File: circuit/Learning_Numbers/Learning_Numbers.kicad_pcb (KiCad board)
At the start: 2 copper layers, 141 x 124 mm, 106 parts, among them SW1 SW_DIP_x01, SW10 SW_Push, SW11 SW_Push, SW12 SW_Push, SW13 SW_Push, SW14 SW_Push, SW15 SW_Push, SW16 SW_Push, SW17 SW_Push, SW18 SW_Push, SW19 SW_Push, SW2 SW_Push, SW20 SW_Push, SW21 SW_Push, SW22 SW_Push, SW23 SW_Push, SW3 SW_Push, SW4 SW_Push, SW5 SW_Push, SW6 SW_Push, SW7 SW_Push, SW8 SW_Push, SW9 SW_Push, U1 ATmega168PA-P, U2 74HC165, U3 74HC165, U4 74HC595, U5 74HC595, U6 74HC595, U7 74HC595, U8 74HC595

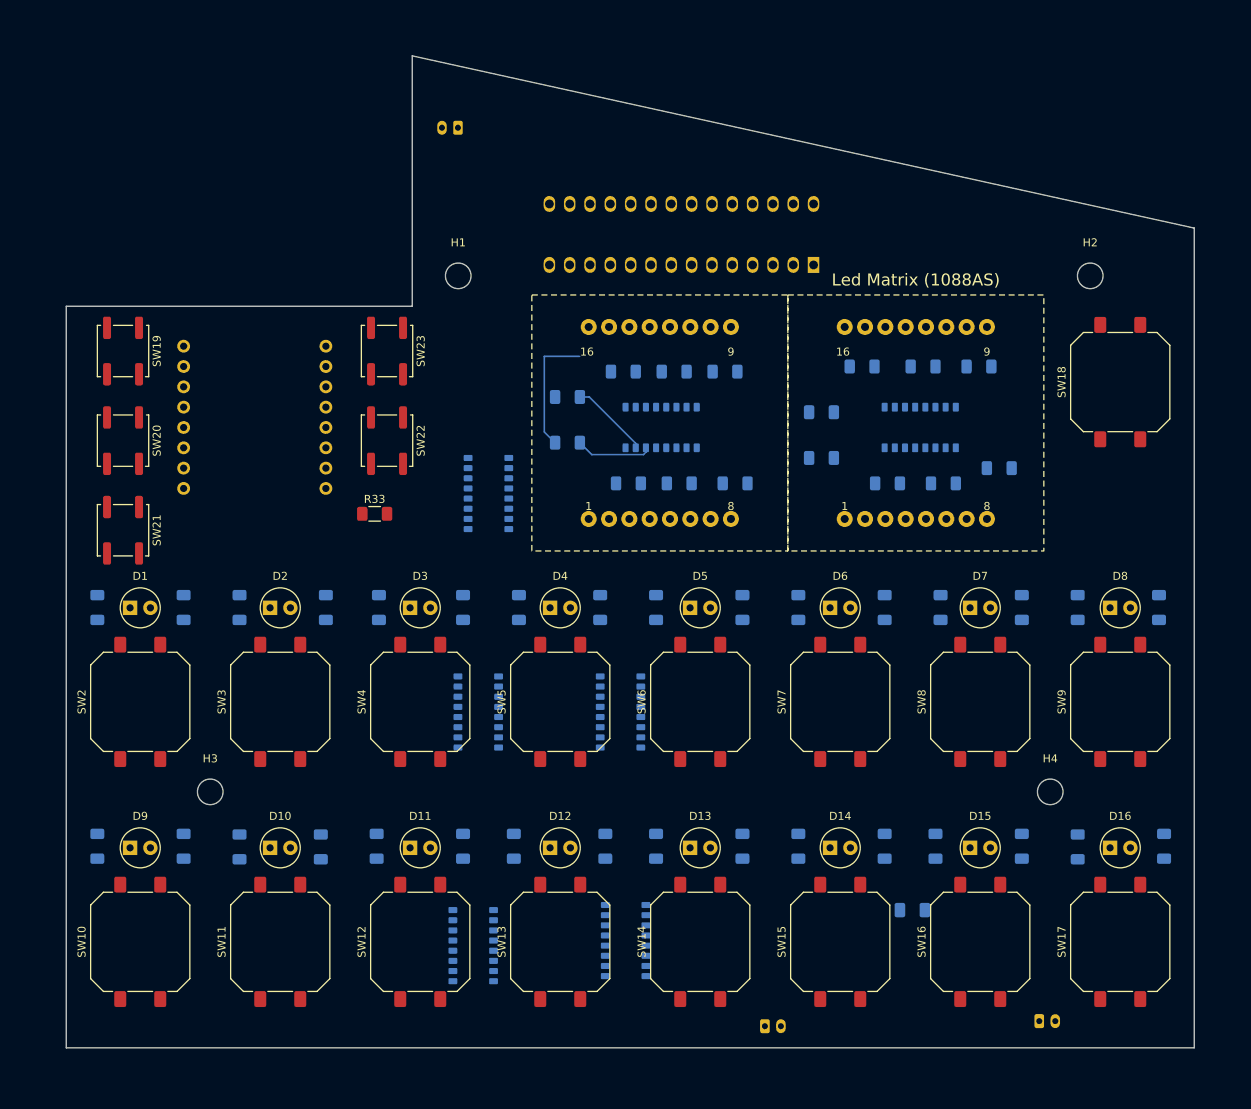
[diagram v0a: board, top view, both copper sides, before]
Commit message: finish circuit pathing
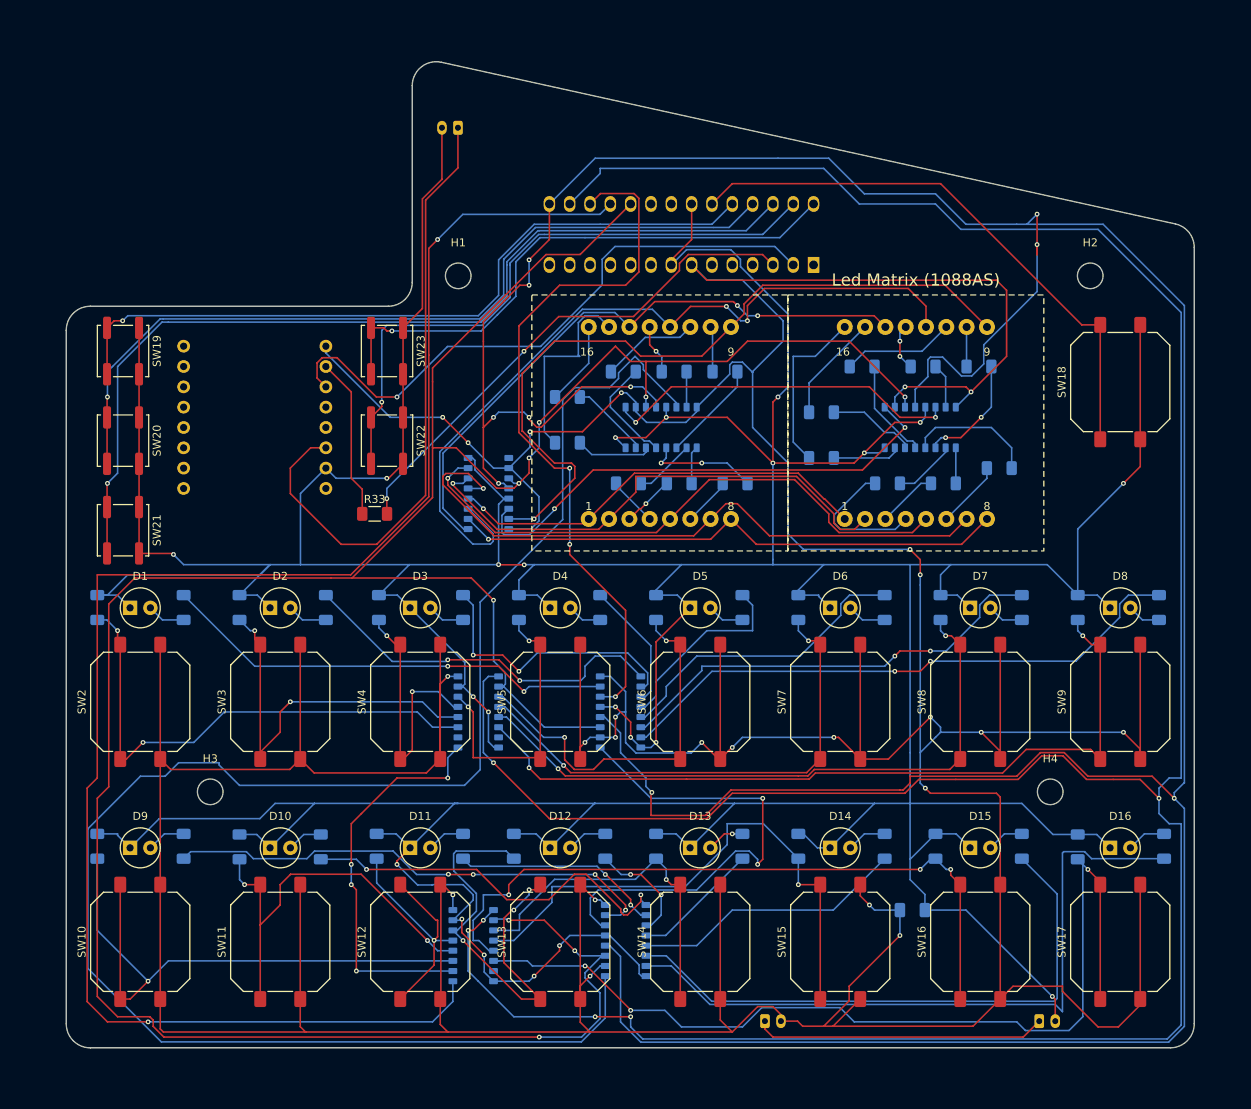
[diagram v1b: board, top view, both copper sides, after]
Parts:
- moved SW1 0.63 mm to (139.3, 158.7)
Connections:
- U4 pad 12: unconnected-(U4-RCLK-Pad12) -> LATCH
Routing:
- net GND: track 0.00 -> 851.2 mm, vias 0 -> 22
- net VCC: track 0.00 -> 846.9 mm, vias 0 -> 24
- net LATCH: track 0.00 -> 460.4 mm, vias 0 -> 10
- net PL: track 0.00 -> 387.1 mm, vias 0 -> 6
- net CLOCK: track 0.00 -> 367.8 mm, vias 0 -> 9
- net Net-(U4-SER): track 0.00 -> 217.7 mm
- net Net-(U1-PB4): track 0.00 -> 205.8 mm, vias 0 -> 2
- net Switch16: track 0.00 -> 119.2 mm, vias 0 -> 3
- net PC3: track 0.00 -> 116.8 mm, vias 0 -> 1
- net PC2: track 0.00 -> 103.5 mm, vias 0 -> 1
- net Switch8: track 0.00 -> 99.9 mm, vias 0 -> 2
- net row4: track 0.00 -> 98.5 mm, vias 0 -> 2
- net row1: track 0.00 -> 94.6 mm, vias 0 -> 1
- net PC1: track 0.00 -> 93.0 mm, vias 0 -> 1
- net SER: track 0.00 -> 89.3 mm, vias 0 -> 3
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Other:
- board size 141 x 124 mm -> 141 x 123.3 mm

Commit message: add crystal to circuit
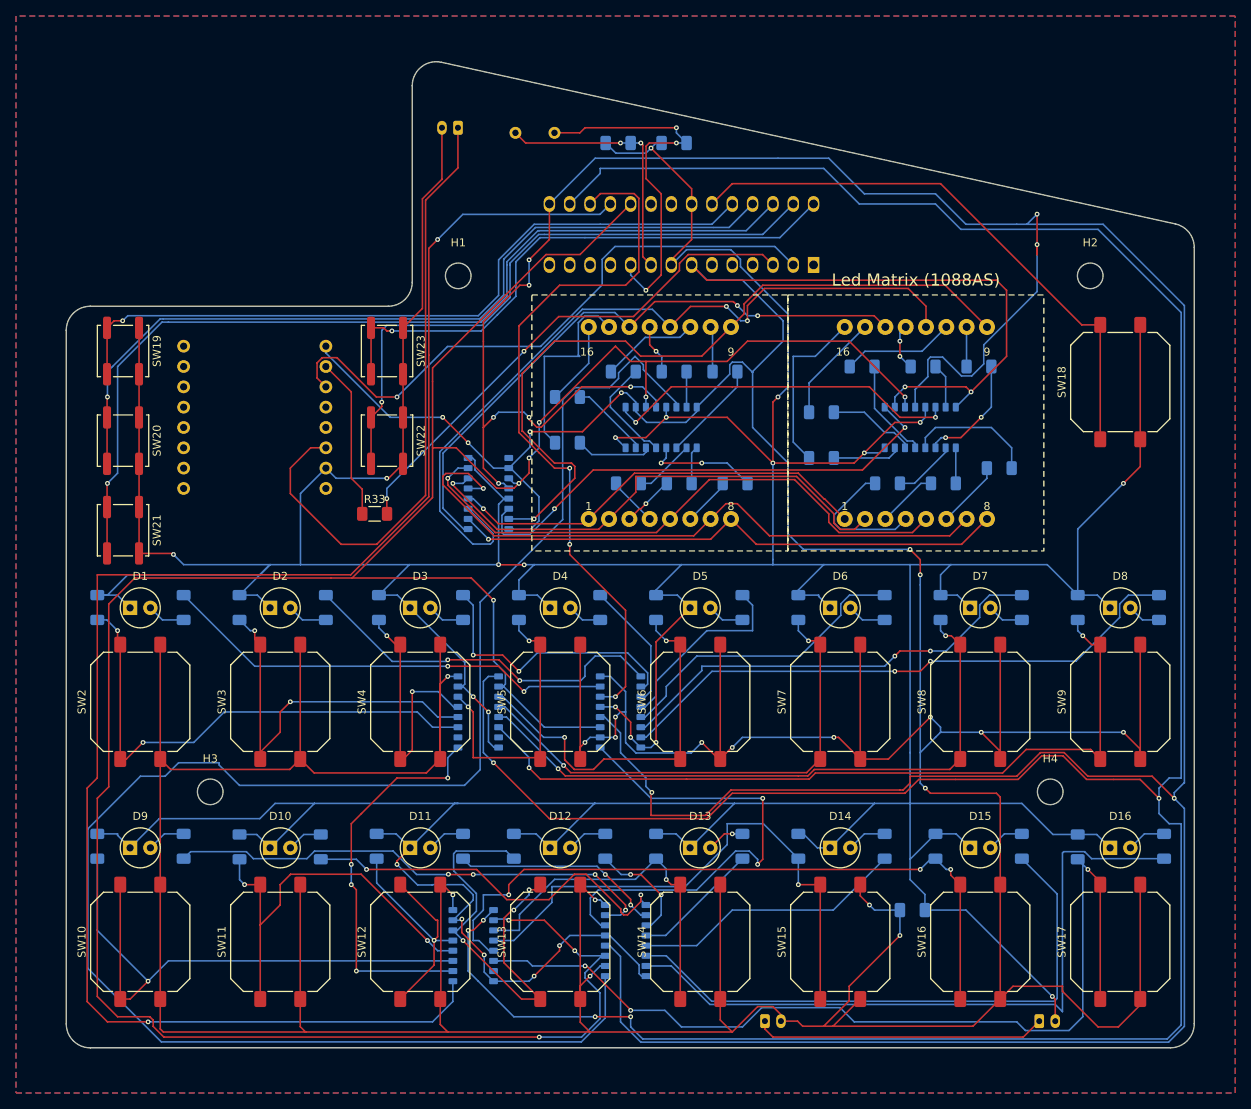
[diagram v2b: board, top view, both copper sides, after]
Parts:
- added C2: 22pf, Capacitor_SMD:C_1206_3216Metric_Pad1.33x1.80mm_HandSolder, B.Cu at (121.0, 48.9)
- added C3: 22pf, Capacitor_SMD:C_1206_3216Metric_Pad1.33x1.80mm_HandSolder, B.Cu at (128.0, 48.9)
- added Y1: 8Mhz, Crystal:Crystal_HC49-4H_Vertical, B.Cu at (113.0, 47.6)
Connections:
- U1 pad 10: unconnected-(U1-XTAL2/PB7-Pad10) -> XTAL2
- U1 pad 9: unconnected-(U1-XTAL1/PB6-Pad9) -> XTAL1
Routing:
- net XTAL2: track 0.00 -> 46.7 mm, vias 0 -> 3
- net XTAL1: track 0.00 -> 32.0 mm, vias 0 -> 2
- net GND: track 851.2 -> 868.4 mm, vias 22 -> 23
- added copper zone on B.Cu, net (none)
- added copper zone on F.Cu, net (none)
